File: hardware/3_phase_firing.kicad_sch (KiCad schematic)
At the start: 14 parts

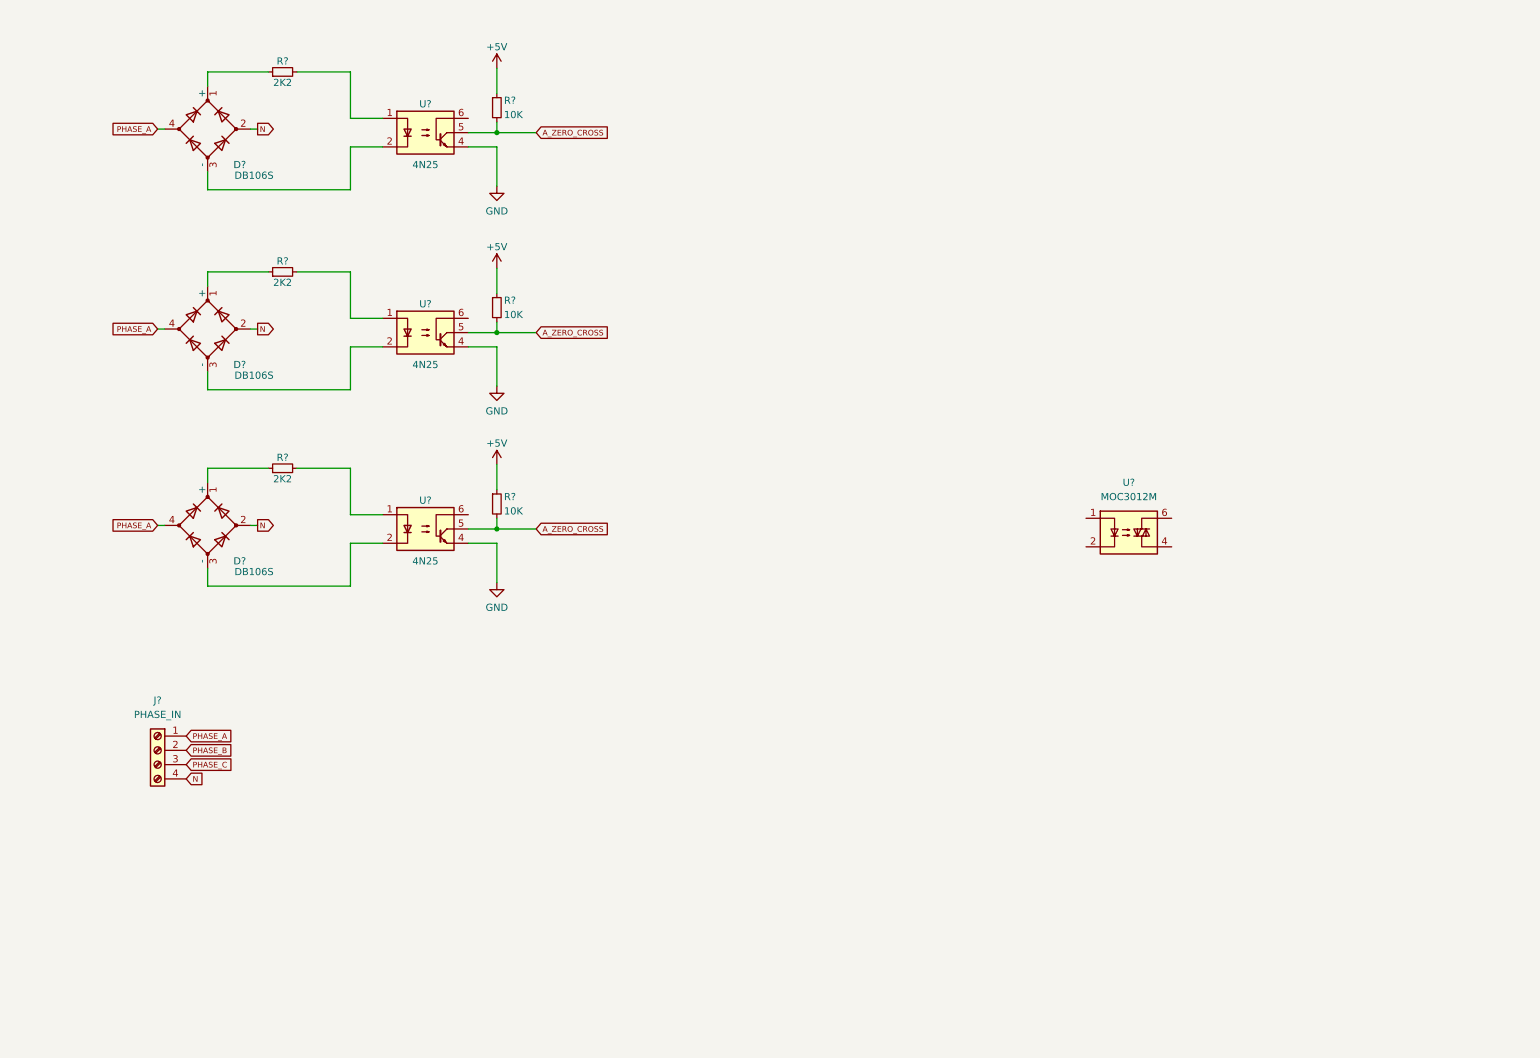
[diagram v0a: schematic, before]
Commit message: completing zero detector circuit
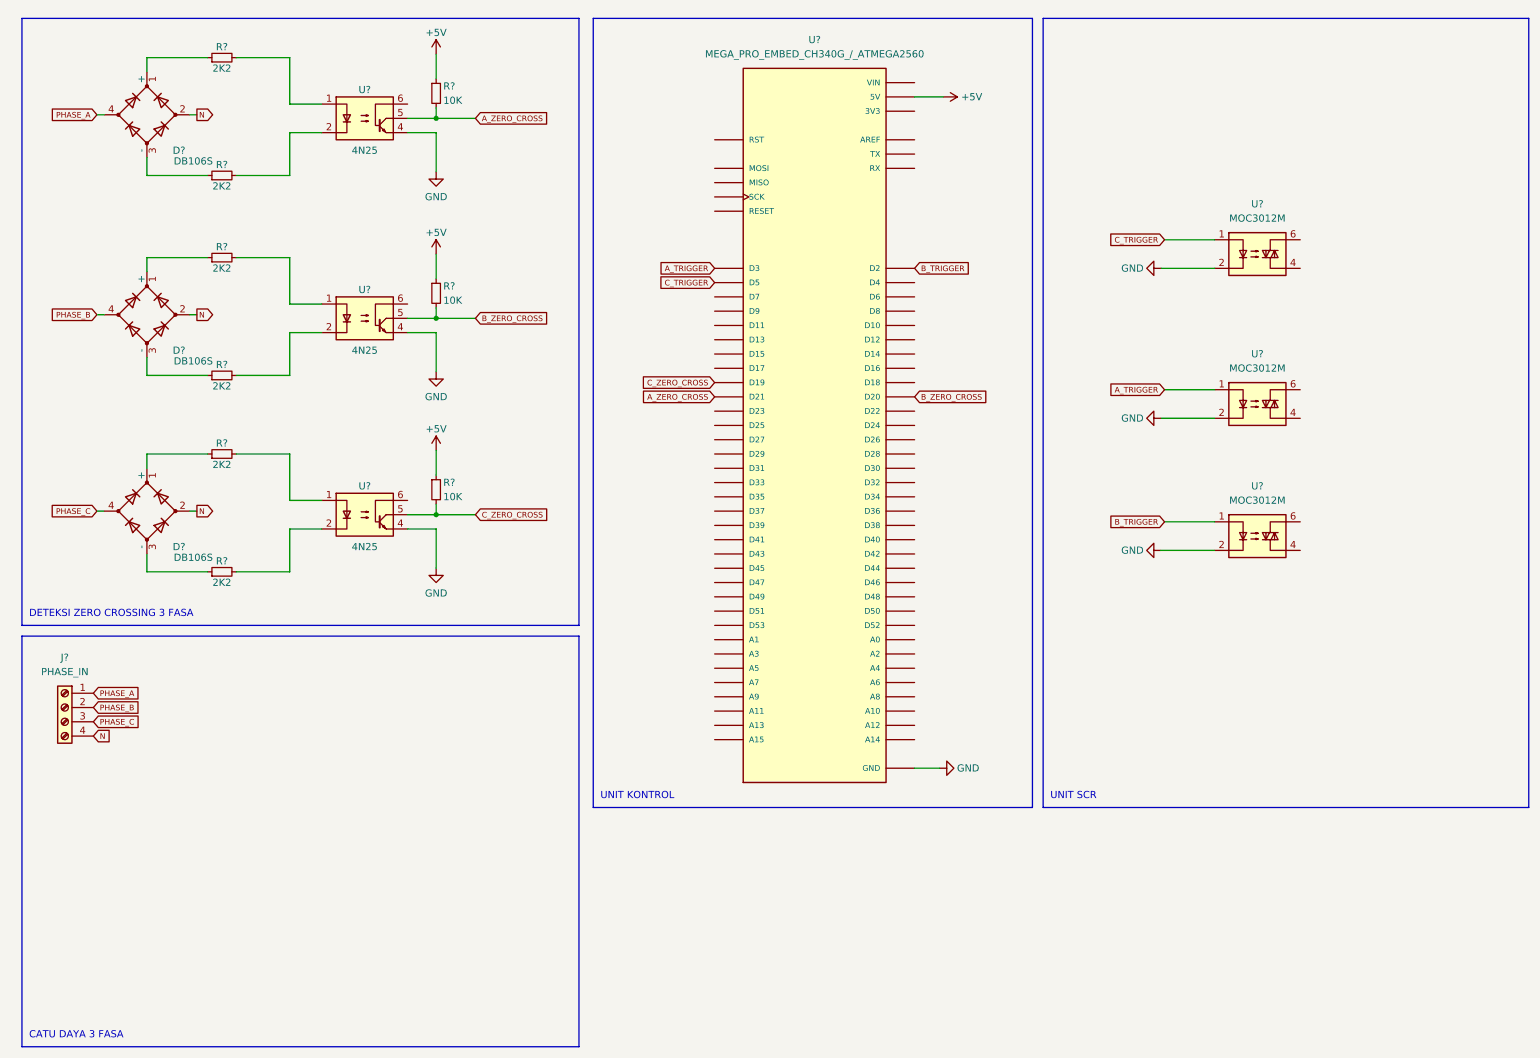
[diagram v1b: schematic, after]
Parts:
- added R? (x3): 2K2, symbol Device:R_Small
- added U? (x2): MOC3012M, symbol Relay_SolidState:MOC3012M
- added U?: MEGA_PRO_EMBED_CH340G_/_ATMEGA2560, MODULE_MEGA_PRO_EMBED_CH340G_/_ATMEGA2560, symbol MEGA_PRO_EMBED_CH340G___ATMEGA2560:MEGA_PRO_EMBED_CH340G_/_ATMEGA2560
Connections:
- net +5V: now also U?.5V_1 (5V), U?.5V_2 (5V), U?.5V_3 (5V)
- net A_ZERO_CROSS: now also U?.D21; no longer R?.2, R?.2, U?.5, U?.5
- net GND: now also U?.2, U?.2, U?.2, U?.GND_1 (GND), U?.GND_2 (GND), U?.GND_3 (GND)
- net PHASE_A: no longer D?.4, D?.4
- net PHASE_B: now also D?.4
- net PHASE_C: now also D?.4
- net C_TRIGGER: now reaches U?.1
- net C_TRIGGER: now also U?.D5
- net at D?.3 (-): now also R?.1; no longer U?.2 (x2)
- net at U?.2: now also R?.2; no longer D?.3 (-)
- new net: R?.2, U?.2 (x2)
- new net: D?.3 (-), R?.1
- new net: U?.3V3_1 (3V3), U?.3V3_2 (3V3)
- new net: U?.VIN_1 (VIN), U?.VIN_2 (VIN)
- new net A_TRIGGER: U?.1, U?.D3
- new net B_TRIGGER: U?.1, U?.D2
- new net B_ZERO_CROSS: R?.2, U?.5, U?.D20
- new net C_ZERO_CROSS: R?.2, U?.5, U?.D19
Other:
- note added: "CATU DAYA 3 FASA"
- note added: "DETEKSI ZERO CROSSING 3 FASA"
- note added: "UNIT KONTROL"
- note added: "UNIT SCR"
- moved on the sheet: D?, J?, R?, U?

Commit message: done with schematic + pcb
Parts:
- removed J?: PHASE_IN, symbol Connector:Screw_Terminal_01x04
- removed U? (x2): MOC3012M, symbol Relay_SolidState:MOC3012M
- added J1: PHASE_IN_1, TerminalBlock:TerminalBlock_bornier-2_P5.08mm, symbol Connector:Screw_Terminal_01x02
- added J2: PHASE_OUT_1, TerminalBlock:TerminalBlock_bornier-2_P5.08mm, symbol Connector:Screw_Terminal_01x02
- added J3: PHASE_IN_2, TerminalBlock:TerminalBlock_bornier-2_P5.08mm, symbol Connector:Screw_Terminal_01x02
- added J4: PHASE_OUT_2, TerminalBlock:TerminalBlock_bornier-2_P5.08mm, symbol Connector:Screw_Terminal_01x02
- added Q1, Q2, Q3: BT136-500, Package_TO_SOT_THT:TO-220-3_Vertical, symbol Triac_Thyristor:BT136-500
- added R10, R11, R12, R13, R14, R15: 330, Resistor_SMD:R_1206_3216Metric_Pad1.30x1.75mm_HandSolder, symbol Device:R_Small
- added U6, U7: MOC3012M, Package_DIP:DIP-6_W8.89mm_SMDSocket_LongPads, symbol Relay_SolidState:MOC3012M
- D1, D2, D3: renamed from D?; footprint (none) -> Diode_SMD:Diode_Bridge_OnSemi_SDIP-4L
- R1, R2, R3, R4, R5, R6, R7, R8, R9: renamed from R?; footprint (none) -> Resistor_SMD:R_1206_3216Metric_Pad1.30x1.75mm_HandSolder
- U1, U2, U3: renamed from U?; footprint Package_DIP:DIP-6_W7.62mm -> Package_DIP:DIP-6_W8.89mm_SMDSocket_LongPads
- U4: renamed from U?; footprint MODULE_MEGA_PRO_EMBED_CH340G_/_ATMEGA2560 -> MEGA_PRO_EMBED_CH340G___ATMEGA2560:MODULE_MEGA_PRO_EMBED_CH340G___ATMEGA2560
- U5: renamed from U?; footprint (none) -> Package_DIP:DIP-6_W8.89mm_SMDSocket_LongPads
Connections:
- net A_TRIGGER: now also U5.1
- net B_TRIGGER: now also U6.1
- net C_TRIGGER: now also U7.1; no longer U5.1
- net GND: now also U6.2, U7.2
- net N: now also J3.2 (Pin_2), J4.2 (Pin_2)
- net PHASE_A: now also J1.1 (Pin_1), Q1.2 (A2), R10.2
- net PHASE_B: now also J1.2 (Pin_2), Q2.2 (A2), R12.2
- net PHASE_C: now also J3.1 (Pin_1), Q3.2 (A2), R14.2
- net at U5.4: now also R11.1
- net at U5.6: now also R10.1
- new net: Q2.3 (G), R13.2
- new net: R15.1, U7.4
- new net: R14.1, U7.6
- new net: Q3.3 (G), R15.2
- new net: R13.1, U6.4
- new net: R12.1, U6.6
- new net: Q1.3 (G), R11.2
- new net OUT_A: J2.1 (Pin_1), Q1.1 (A1)
- new net OUT_B: J2.2 (Pin_2), Q2.1 (A1)
- new net OUT_C: J4.1 (Pin_1), Q3.1 (A1)
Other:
- moved on the sheet: U5

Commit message: updating gitignore
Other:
- note added: "MODUL ELDA PEMICU OPTIK 3 FASA"

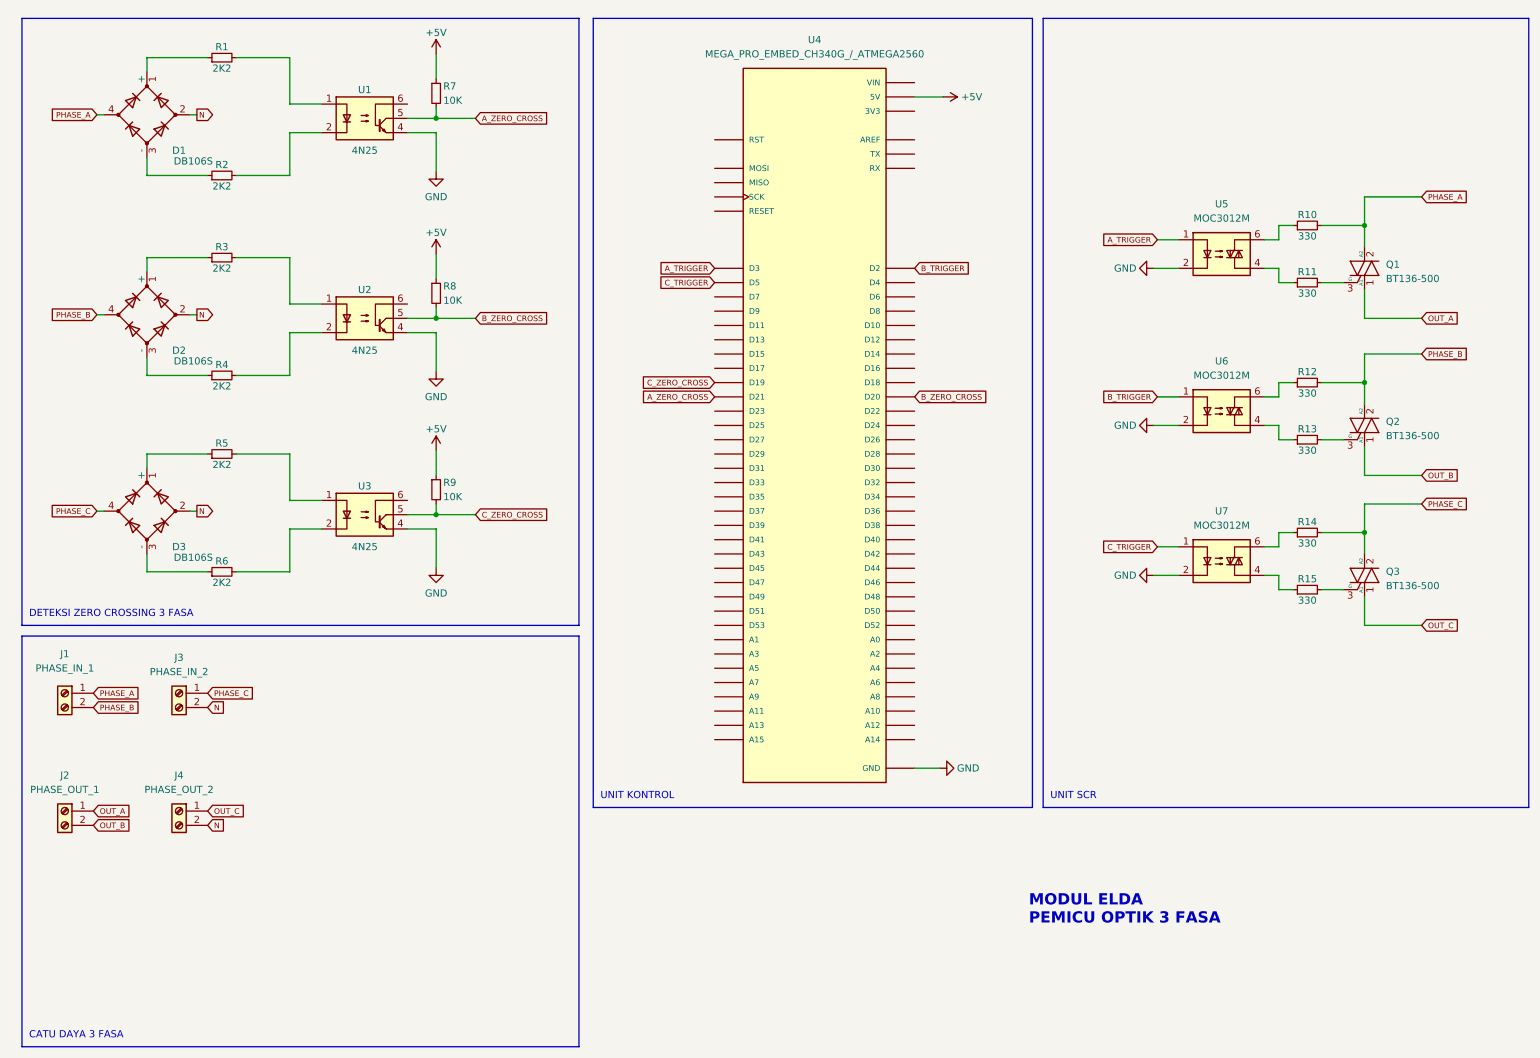
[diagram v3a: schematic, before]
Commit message: modifying footprint
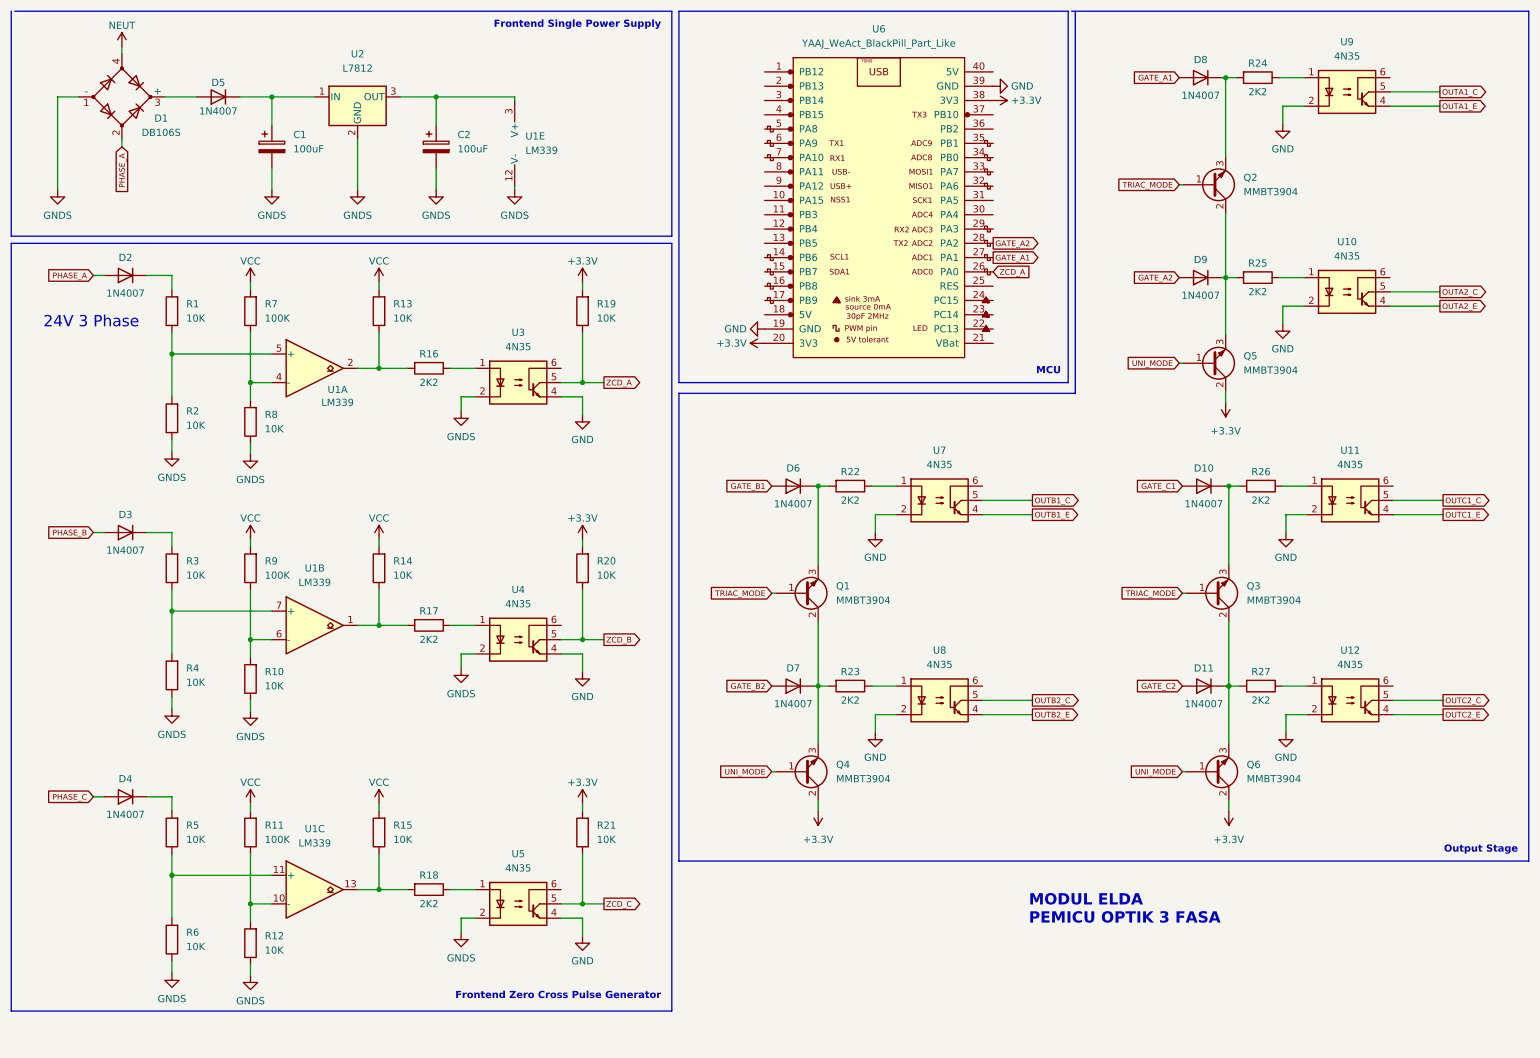
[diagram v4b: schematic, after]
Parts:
- removed D1, D2, D3: DB106S, Diode_SMD:Diode_Bridge_OnSemi_SDIP-4L, symbol Device:D_Bridge_+A-A
- removed J1: PHASE_IN_1, TerminalBlock:TerminalBlock_bornier-2_P5.08mm, symbol Connector:Screw_Terminal_01x02
- removed J2: PHASE_OUT_1, TerminalBlock:TerminalBlock_bornier-2_P5.08mm, symbol Connector:Screw_Terminal_01x02
- removed J3: PHASE_IN_2, TerminalBlock:TerminalBlock_bornier-2_P5.08mm, symbol Connector:Screw_Terminal_01x02
- removed J4: PHASE_OUT_2, TerminalBlock:TerminalBlock_bornier-2_P5.08mm, symbol Connector:Screw_Terminal_01x02
- removed Q1, Q2, Q3: BT136-500, Package_TO_SOT_THT:TO-220-3_Vertical, symbol Triac_Thyristor:BT136-500
- removed R1, R2, R3, R4, R5, R6: 2K2, Resistor_SMD:R_1206_3216Metric_Pad1.30x1.75mm_HandSolder, symbol Device:R_Small
- removed R10, R11, R12, R13, R14, R15: 330, Resistor_SMD:R_1206_3216Metric_Pad1.30x1.75mm_HandSolder, symbol Device:R_Small
- removed R7, R8, R9: 10K, Resistor_SMD:R_1206_3216Metric_Pad1.30x1.75mm_HandSolder, symbol Device:R_Small
- removed U1, U2, U3: 4N25, Package_DIP:DIP-6_W8.89mm_SMDSocket_LongPads, symbol Isolator:4N25
- removed U4: MEGA_PRO_EMBED_CH340G_/_ATMEGA2560, MEGA_PRO_EMBED_CH340G___ATMEGA2560:MODULE_MEGA_PRO_EMBED_CH340G___ATMEGA2560, symbol MEGA_PRO_EMBED_CH340G___ATMEGA2560:MEGA_PRO_EMBED_CH340G_/_ATMEGA2560
- removed U5, U6, U7: MOC3012M, Package_DIP:DIP-6_W8.89mm_SMDSocket_LongPads, symbol Relay_SolidState:MOC3012M
- added C1, C2: 100uF, Capacitor_SMD:CP_Elec_6.3x7.7, symbol Device:C_Polarized
- added D1: DB106S, Diode_SMD:Diode_Bridge_OnSemi_SDIP-4L, symbol Device:D_Bridge_-A+A
- added D10, D11, D2, D3, D4, D5, D6, D7, D8, D9: 1N4007, Diode_SMD:D_SMA_Handsoldering, symbol Device:D
- added Q1, Q2, Q3, Q4, Q5, Q6: MMBT3904, Package_TO_SOT_SMD:SOT-23, symbol Device:Q_NPN_BCE
- added R1, R10, R12, R13, R14, R15, R19, R2, R20, R21, R3, R4, R5, R6, R8: 10K, Resistor_SMD:R_0805_2012Metric, symbol Device:R
- added R11, R7, R9: 100K, Resistor_SMD:R_0805_2012Metric, symbol Device:R
- added R16, R17, R18, R22, R23, R24, R25, R26, R27: 2K2, Resistor_SMD:R_0805_2012Metric, symbol Device:R
- added U1: LM339, Package_SO:SOIC-14_3.9x8.7mm_P1.27mm, symbol Comparator:LM339
- added U10, U11, U12, U3, U4, U5, U7, U8, U9: 4N35, Package_DIP:DIP-6_W8.89mm_SMDSocket_LongPads, symbol Isolator:4N35
- added U2: L7812, Package_TO_SOT_SMD:TO-263-2, symbol Regulator_Linear:L7812
- added U6: YAAJ_WeAct_BlackPill_Part_Like, Footprints:YAAJ_WeAct_BlackPill_2, symbol YAAJ_WeAct_BlackPill_Part_Like:YAAJ_WeAct_BlackPill_Part_Like
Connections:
- net GND: now also U10.2, U11.2, U12.2, U3.4, U4.4, U5.4, U6.19 (GND), U6.39 (GND), U7.2, U8.2, U9.2
- net PHASE_A: now also D1.2, D2.2 (A)
- net PHASE_B: now also D3.2 (A)
- net PHASE_C: now also D4.2 (A)
- new net: R16.1, U3.1
- new net: R7.1, R8.2, U1.4 (-)
- new net: R5.1, R6.2, U1.11 (+)
- new net: C1.1, D5.1 (K), U2.1 (IN)
- new net: C2.1, U1.3 (V+), U2.3 (OUT)
- new net: R15.1, R18.2, U1.13
- new net: R18.1, U5.1
- new net: R11.1, R12.2, U1.10 (-)
- new net: R17.1, U4.1
- new net: R14.1, R17.2, U1.1
- new net: D2.1 (K), R1.2
- new net: R10.2, R9.1, U1.6 (-)
- new net: D7.1 (K), Q1.2 (C), Q4.3 (E), R23.2
- new net: D11.1 (K), Q3.2 (C), Q6.3 (E), R27.2
- new net: R24.1, U9.1
- new net: D8.1 (K), Q2.3 (E), R24.2
- new net: D9.1 (K), Q2.2 (C), Q5.3 (E), R25.2
- new net: D1.3 (+), D5.2 (A)
- new net: R25.1, U10.1
- new net: D4.1 (K), R5.2
- new net: R22.1, U7.1
- new net: R26.1, U11.1
- new net: D10.1 (K), Q3.3 (E), R26.2
- new net: R3.1, R4.2, U1.7 (+)
- new net: D3.1 (K), R3.2
- new net: R27.1, U12.1
- new net: R23.1, U8.1
- new net: D6.1 (K), Q1.3 (E), R22.2
- new net: R1.1, R2.2, U1.5 (+)
- new net: R13.1, R16.2, U1.2
- new net +3.3V: Q4.2 (C), Q5.2 (C), Q6.2 (C), R19.2, R20.2, R21.2, U6.20 (3V3), U6.38 (3V3)
- new net GATE_A1: D8.2 (A), U6.27 (PA1)
- new net GATE_A2: D9.2 (A), U6.28 (PA2)
- new net GATE_B1: D6.2 (A)
- new net GATE_B2: D7.2 (A)
- new net GATE_C1: D10.2 (A)
- new net GATE_C2: D11.2 (A)
- new net GNDS: C1.2, C2.2, D1.1 (-), R10.1, R12.1, R2.1, R4.1, R6.1, R8.1, U1.12 (V-), U2.2 (GND), U3.2, U4.2, U5.2
- new net NEUT: D1.4
- new net OUTA1_C: U9.5
- new net OUTA1_E: U9.4
- new net OUTA2_C: U10.5
- new net OUTA2_E: U10.4
- new net OUTB1_C: U7.5
- new net OUTB1_E: U7.4
- new net OUTB2_C: U8.5
- new net OUTB2_E: U8.4
- new net OUTC1_C: U11.5
- new net OUTC1_E: U11.4
- new net OUTC2_C: U12.5
- new net OUTC2_E: U12.4
- new net TRIAC_MODE: Q1.1 (B), Q2.1 (B), Q3.1 (B)
- new net UNI_MODE: Q4.1 (B), Q5.1 (B), Q6.1 (B)
- new net VCC: R11.2, R13.2, R14.2, R15.2, R7.2, R9.2
- new net ZCD_A: R19.1, U3.5, U6.26 (PA0)
- new net ZCD_B: R20.1, U4.5
- new net ZCD_C: R21.1, U5.5
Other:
- note added: "24V 3 Phase"
- note added: "Frontend Single Power Supply"
- note added: "Frontend Zero Cross Pulse Generator"
- note added: "MCU"
- note added: "Output Stage"
- note removed: "CATU DAYA 3 FASA"
- note removed: "DETEKSI ZERO CROSSING 3 FASA"
- note removed: "UNIT KONTROL"
- note removed: "UNIT SCR"

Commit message: done with pcb layouting, routing need to done more
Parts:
- added J1: IN1, TerminalBlock:TerminalBlock_bornier-2_P5.08mm, symbol Connector:Screw_Terminal_01x02
- added J2: IN2, TerminalBlock:TerminalBlock_bornier-2_P5.08mm, symbol Connector:Screw_Terminal_01x02
- added J3: OUT, TerminalBlock_Phoenix:TerminalBlock_Phoenix_MKDS-3-12-5.08_1x12_P5.08mm_Horizontal, symbol Connector:Screw_Terminal_01x12
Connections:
- net NEUT: now also J1.1 (Pin_1)
- net OUTA1_C: now also J3.12 (Pin_12)
- net OUTA1_E: now also J3.11 (Pin_11)
- net OUTA2_C: now also J3.10 (Pin_10)
- net OUTA2_E: now also J3.9 (Pin_9)
- net OUTB1_C: now also J3.8 (Pin_8)
- net OUTB1_E: now also J3.7 (Pin_7)
- net OUTB2_C: now also J3.6 (Pin_6)
- net OUTB2_E: now also J3.5 (Pin_5)
- net OUTC1_C: now also J3.4 (Pin_4)
- net OUTC1_E: now also J3.3 (Pin_3)
- net OUTC2_C: now also J3.2 (Pin_2)
- net OUTC2_E: now also J3.1 (Pin_1)
- net PHASE_A: now also J1.2 (Pin_2)
- net PHASE_B: now also J2.1 (Pin_1)
- net PHASE_C: now also J2.2 (Pin_2)
- net VCC: now also C2.1, U1.3 (V+), U2.3 (OUT)
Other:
- moved on the sheet: D10, D11, D8, D9, Q2, Q3, Q5, Q6, R24, R25, R26, R27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
